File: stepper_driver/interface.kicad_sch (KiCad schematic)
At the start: 17 parts, among them J1 Conn_FFC_20_Pin, J2 Conn_TERM_HDR_01x08_Pin_3.5MM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, U2 MAX6817, U3 LTC2854CDD, U4 SN65LVDM050QDRQ1

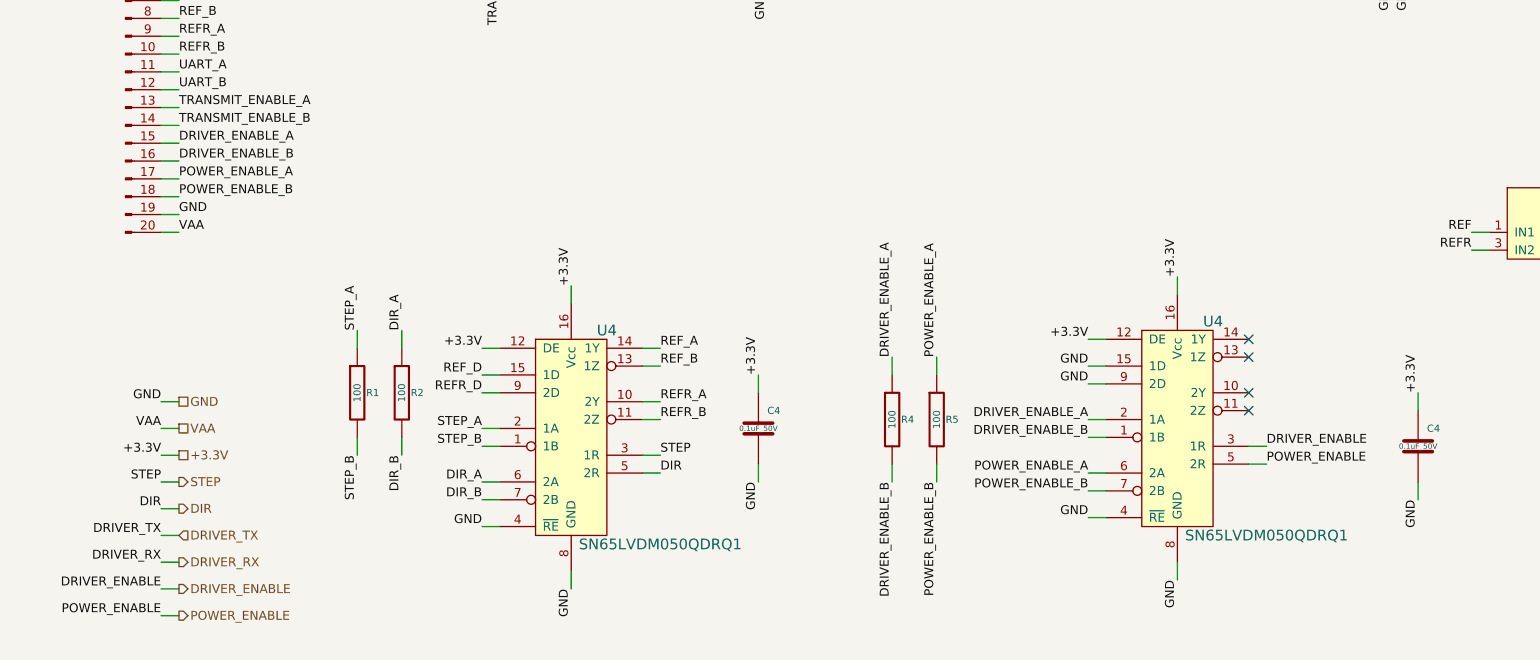
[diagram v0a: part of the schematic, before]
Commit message: Add power enable circuitry
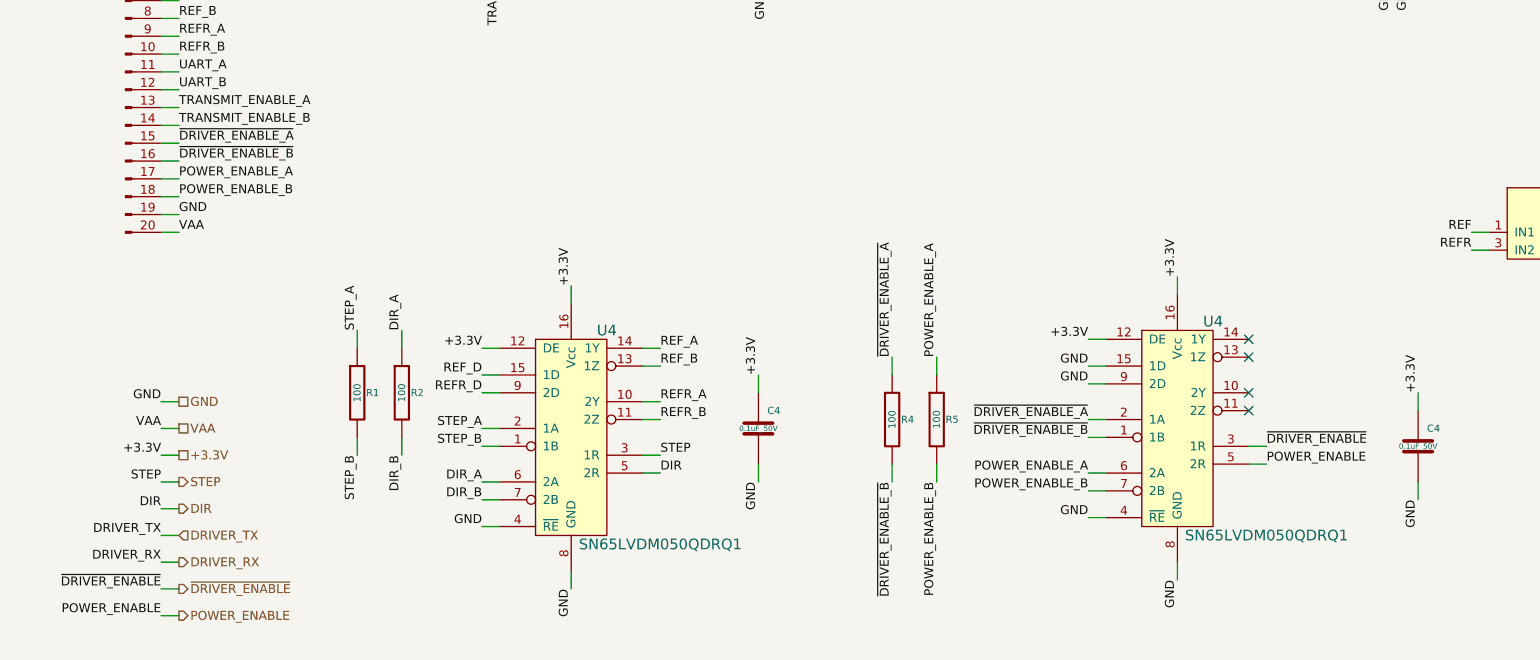
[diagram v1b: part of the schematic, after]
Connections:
- net DRIVER_ENABLE renamed ~{DRIVER_ENABLE}
- net DRIVER_ENABLE_A renamed ~{DRIVER_ENABLE_A}
- net DRIVER_ENABLE_B renamed ~{DRIVER_ENABLE_B}
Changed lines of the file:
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@@
   (title_block
     (title "stepper_driver")
-    (date "2023-05-03")
+    (date "2023-05-04")
     (rev "2.0")
     (company "Howard Hughes Medical Institute")
@@
     (effects (font (size 1.27 1.27)) (justify right bottom))
   )
-  (label "DRIVER_ENABLE_B" (at 139.7 137.16 270) (fields_autoplaced)
-    (effects (font (size 1.27 1.27)) (justify right bottom))
-  )
-  (label "DRIVER_ENABLE_A" (at 38.1 88.9 0) (fields_autoplaced)
+  (label "~{DRIVER_ENABLE_B}" (at 139.7 137.16 270) (fields_autoplaced)
+    (effects (font (size 1.27 1.27)) (justify right bottom))
+  )
+  (label "~{DRIVER_ENABLE_A}" (at 38.1 88.9 0) (fields_autoplaced)
     (effects (font (size 1.27 1.27)) (justify left bottom))
   )
@@
     (effects (font (size 1.27 1.27)) (justify right bottom))
   )
-  (label "DRIVER_ENABLE" (at 35.56 152.4 180) (fields_autoplaced)
+  (label "~{DRIVER_ENABLE}" (at 35.56 152.4 180) (fields_autoplaced)
     (effects (font (size 1.27 1.27)) (justify right bottom))
   )
@@
     (effects (font (size 1.27 1.27)) (justify right bottom))
   )
-  (label "DRIVER_ENABLE" (at 193.04 132.08 0) (fields_autoplaced)
+  (label "~{DRIVER_ENABLE}" (at 193.04 132.08 0) (fields_autoplaced)
     (effects (font (size 1.27 1.27)) (justify left bottom))
   )
@@
     (effects (font (size 1.27 1.27)) (justify left bottom))
   )
-  (label "DRIVER_ENABLE_A" (at 139.7 119.38 90) (fields_autoplaced)
+  (label "~{DRIVER_ENABLE_A}" (at 139.7 119.38 90) (fields_autoplaced)
     (effects (font (size 1.27 1.27)) (justify left bottom))
   )
@@
     (effects (font (size 1.27 1.27)) (justify right bottom))
   )
-  (label "DRIVER_ENABLE_B" (at 167.64 130.81 180) (fields_autoplaced)
-    (effects (font (size 1.27 1.27)) (justify right bottom))
-  )
-  (label "DRIVER_ENABLE_A" (at 167.64 128.27 180) (fields_autoplaced)
+  (label "~{DRIVER_ENABLE_B}" (at 167.64 130.81 180) (fields_autoplaced)
+    (effects (font (size 1.27 1.27)) (justify right bottom))
+  )
+  (label "~{DRIVER_ENABLE_A}" (at 167.64 128.27 180) (fields_autoplaced)
     (effects (font (size 1.27 1.27)) (justify right bottom))
   )
@@
     (effects (font (size 1.27 1.27)) (justify right bottom))
   )
-  (label "DRIVER_ENABLE_B" (at 38.1 91.44 0) (fields_autoplaced)
+  (label "~{DRIVER_ENABLE_B}" (at 38.1 91.44 0) (fields_autoplaced)
     (effects (font (size 1.27 1.27)) (justify left bottom))
   )
@@
     (effects (font (size 1.27 1.27)) (justify left))
   )
-  (hierarchical_label "DRIVER_ENABLE" (shape output) (at 38.1 152.4 0) (fields_autoplaced)
+  (hierarchical_label "~{DRIVER_ENABLE}" (shape output) (at 38.1 152.4 0) (fields_autoplaced)
     (effects (font (size 1.27 1.27)) (justify left))
   )

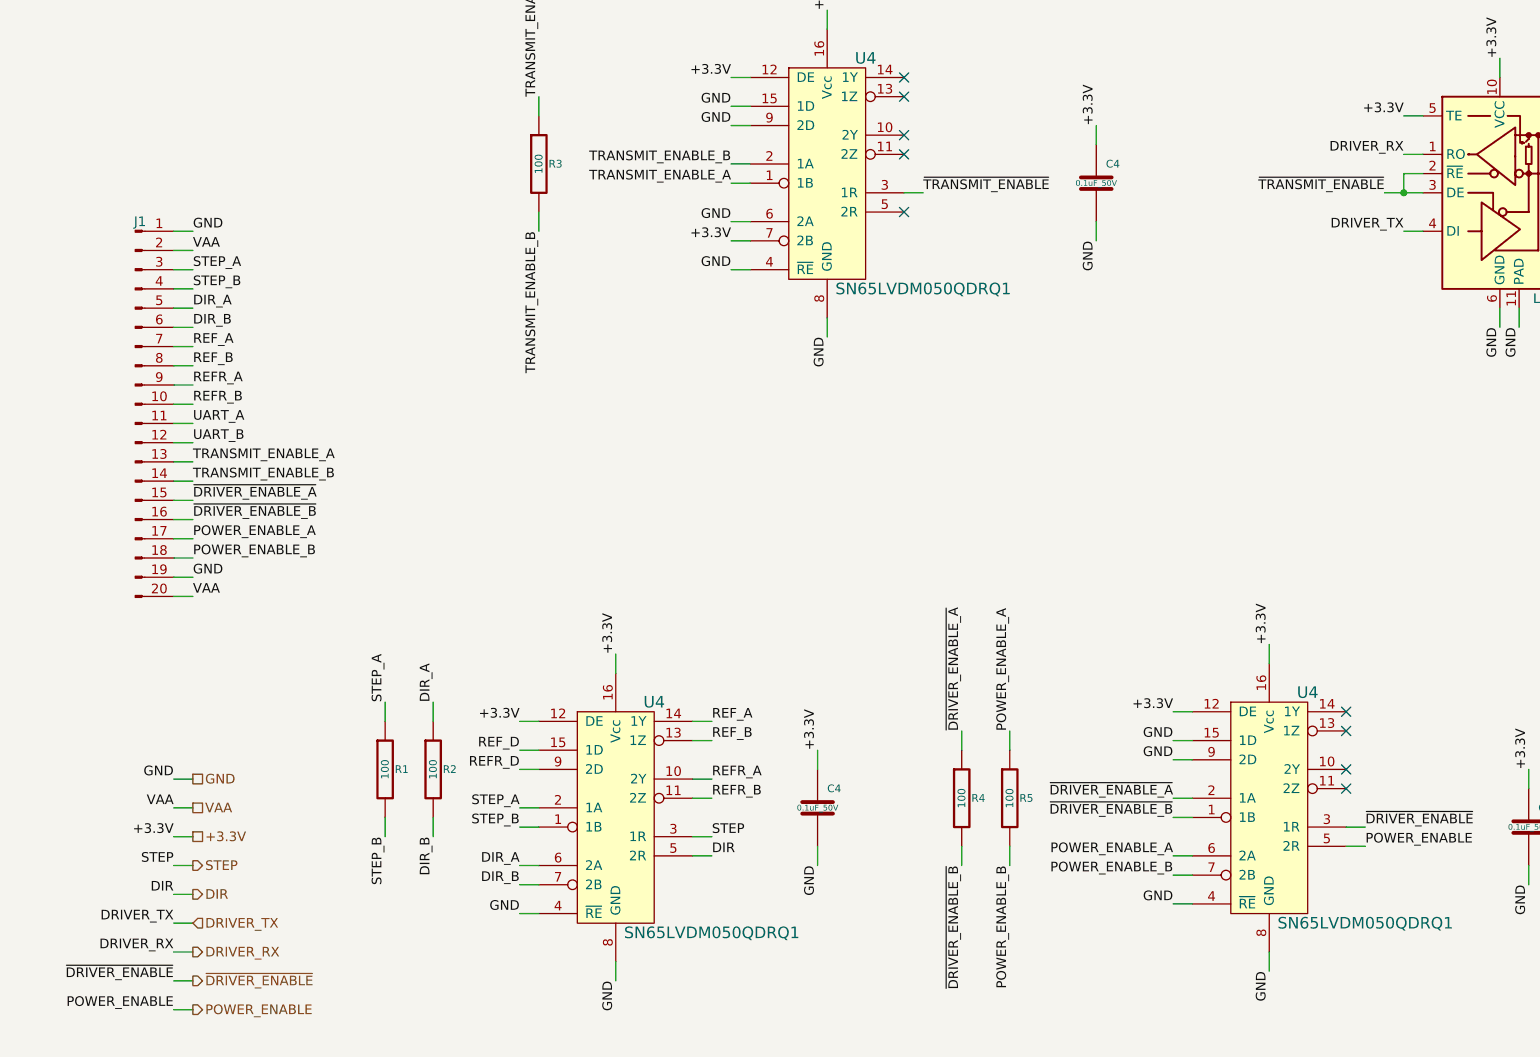
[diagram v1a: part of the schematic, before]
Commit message: Add parts and rename lines
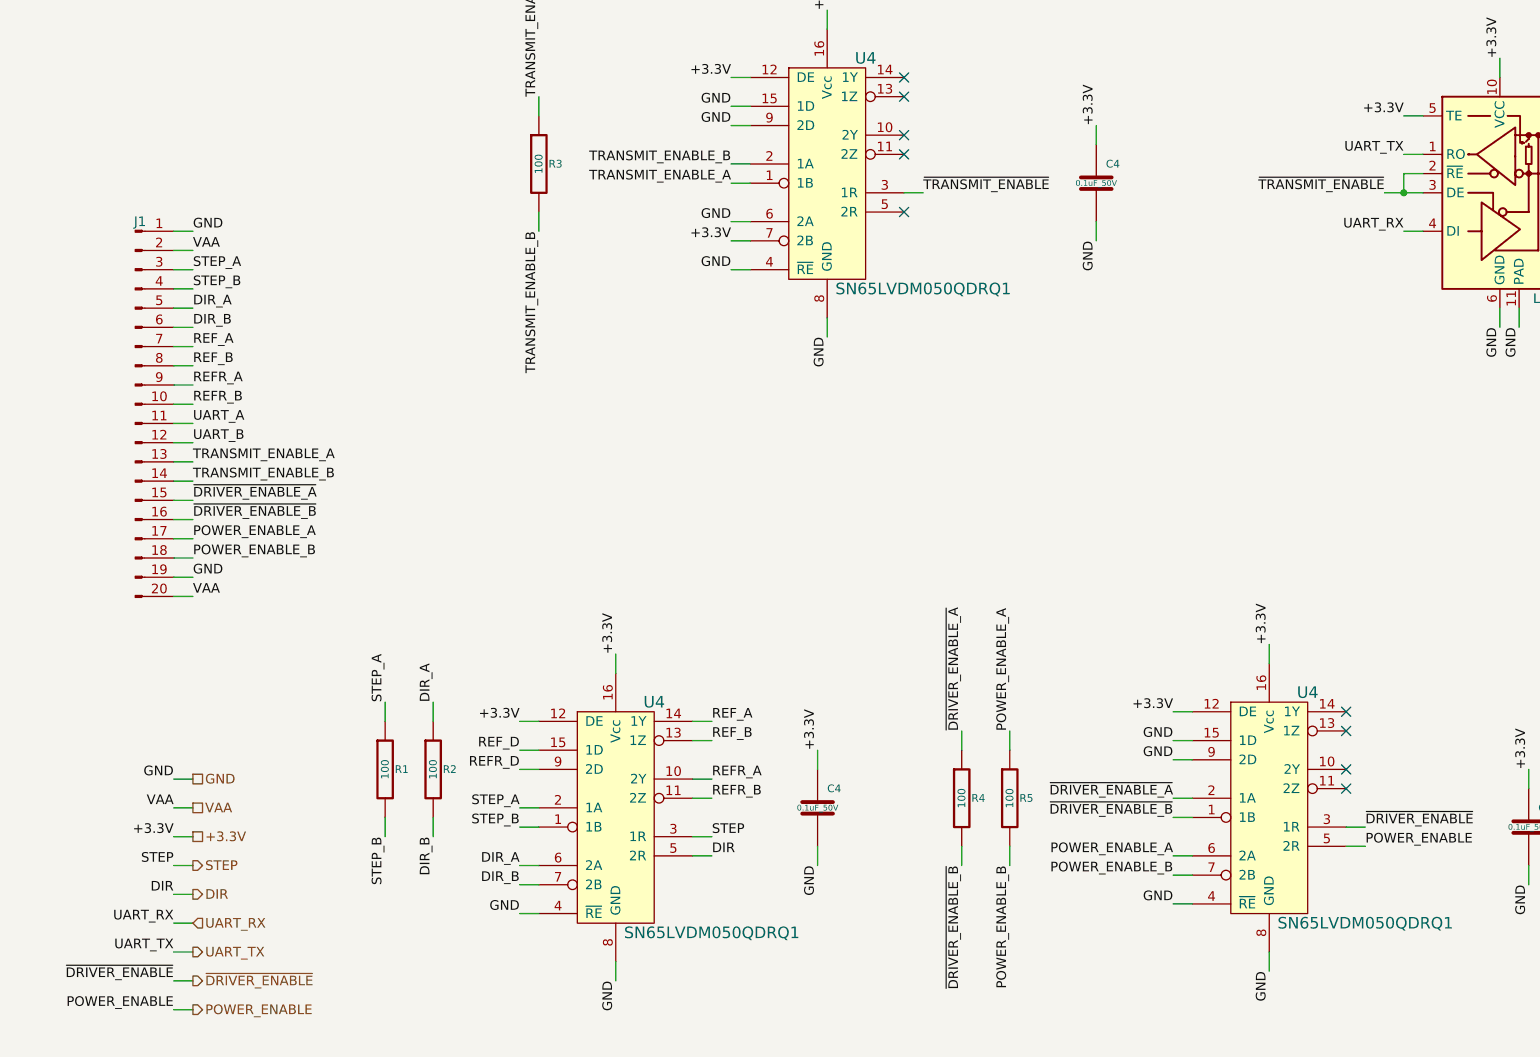
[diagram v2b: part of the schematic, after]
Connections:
- net DRIVER_RX renamed UART_TX
- net DRIVER_TX renamed UART_RX
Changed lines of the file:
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@@
   (title_block
     (title "stepper_driver")
-    (date "2023-05-04")
+    (date "2023-05-05")
     (rev "2.0")
     (company "Howard Hughes Medical Institute")
@@
     (effects (font (size 1.27 1.27)) (justify left bottom))
   )
-  (label "DRIVER_RX" (at 198.12 43.18 180) (fields_autoplaced)
+  (label "UART_TX" (at 198.12 43.18 180) (fields_autoplaced)
     (effects (font (size 1.27 1.27)) (justify right bottom))
   )
@@
     (effects (font (size 1.27 1.27)) (justify left bottom))
   )
-  (label "DRIVER_TX" (at 198.12 53.34 180) (fields_autoplaced)
+  (label "UART_RX" (at 198.12 53.34 180) (fields_autoplaced)
     (effects (font (size 1.27 1.27)) (justify right bottom))
   )
@@
     (effects (font (size 1.27 1.27)) (justify right bottom))
   )
-  (label "DRIVER_RX" (at 35.56 148.59 180) (fields_autoplaced)
+  (label "UART_TX" (at 35.56 148.59 180) (fields_autoplaced)
     (effects (font (size 1.27 1.27)) (justify right bottom))
   )
@@
     (effects (font (size 1.27 1.27)) (justify left bottom))
   )
-  (label "DRIVER_TX" (at 35.56 144.78 180) (fields_autoplaced)
+  (label "UART_RX" (at 35.56 144.78 180) (fields_autoplaced)
     (effects (font (size 1.27 1.27)) (justify right bottom))
   )
@@
     (effects (font (size 1.27 1.27)) (justify left))
   )
-  (hierarchical_label "DRIVER_TX" (shape input) (at 38.1 144.78 0) (fields_autoplaced)
+  (hierarchical_label "UART_RX" (shape input) (at 38.1 144.78 0) (fields_autoplaced)
     (effects (font (size 1.27 1.27)) (justify left))
   )
@@
     (effects (font (size 1.27 1.27)) (justify left))
   )
-  (hierarchical_label "DRIVER_RX" (shape output) (at 38.1 148.59 0) (fields_autoplaced)
+  (hierarchical_label "UART_TX" (shape output) (at 38.1 148.59 0) (fields_autoplaced)
     (effects (font (size 1.27 1.27)) (justify left))
   )

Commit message: Change LVDS chips
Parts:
- removed C4: 0.1uF_50V, Janelia:C_0603_1608Metric, symbol Janelia:C_0.1uF_50V_0603
- removed U4 (x2): SN65LVDM050QDRQ1, Janelia:D16-L, symbol Janelia:SN65LVDM050QDRQ1
- added U7: LVDS_4-4_HALF_DS91M040TSQE, Janelia:DS91M040TSQE_NOPB, symbol Janelia:LVDS_4-4_HALF_DS91M040TSQE
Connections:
- net +3.3V: now also U7.11 (VDD), U7.12 (VDD)
- net DIR: now also U7.5 (RO2)
- net DIR_A: now also J1.7 (Pin_7), U7.19 (A2); no longer J1.5 (Pin_5)
- net DIR_B: now also J1.8 (Pin_8), U7.20 (B2); no longer J1.6 (Pin_6)
- net GND: now also J1.17 (Pin_17), J1.18 (Pin_18), U7.13 (~{RE2}), U7.2 (DI0), U7.26 (~{RE0}), U7.28 (~{RE1}), U7.31 (GND), U7.33 (PAD), U7.4 (DI1), U7.6 (DI2); no longer J1.1 (Pin_1), J1.19 (Pin_19)
- net POWER_ENABLE_A: now also J1.15 (Pin_15); no longer J1.17 (Pin_17)
- net POWER_ENABLE_B: now also J1.16 (Pin_16); no longer J1.18 (Pin_18)
- net REFR_A: no longer J1.9 (Pin_9)
- net REFR_B: no longer J1.10 (Pin_10)
- net REF_A: no longer J1.7 (Pin_7)
- net REF_B: no longer J1.8 (Pin_8)
- net STEP: now also U7.3 (RO1)
- net STEP_A: now also J1.5 (Pin_5), U7.21 (A1); no longer J1.3 (Pin_3)
- net STEP_B: now also J1.6 (Pin_6), U7.22 (B1); no longer J1.4 (Pin_4)
- net TRANSMIT_ENABLE_A: no longer J1.13 (Pin_13)
- net TRANSMIT_ENABLE_B: no longer J1.14 (Pin_14)
- net UART_A: now also J1.1 (Pin_1); no longer J1.11 (Pin_11)
- net UART_B: now also J1.2 (Pin_2); no longer J1.12 (Pin_12)
- net VAA: now also J1.19 (Pin_19); no longer J1.2 (Pin_2)
- net ~{DRIVER_ENABLE_A}: now also J1.9 (Pin_9); no longer J1.15 (Pin_15)
- net ~{DRIVER_ENABLE_B}: now also J1.10 (Pin_10); no longer J1.16 (Pin_16)
- net ~{TRANSMIT_ENABLE} renamed ~{UART_TX_ENABLE}
- net ~{UART_TX_ENABLE}: now also U7.1 (RO0)
- new net ~{UART_TX_ENABLE_A}: J1.3 (Pin_3), U7.23 (A0)
- new net ~{UART_TX_ENABLE_B}: J1.4 (Pin_4), U7.24 (B0)
- no-connect marks 9 -> 7
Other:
- moved on the sheet: C4, J2, R1, R2, R3, R4, R5, U2, U3, U4
